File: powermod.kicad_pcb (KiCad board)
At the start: 4 copper layers, 27 x 18 mm, 21 parts, among them J1 Conn_02x07_Odd_Even, J2 Conn_02x07_Odd_Even, U1 TPS54260DGQ

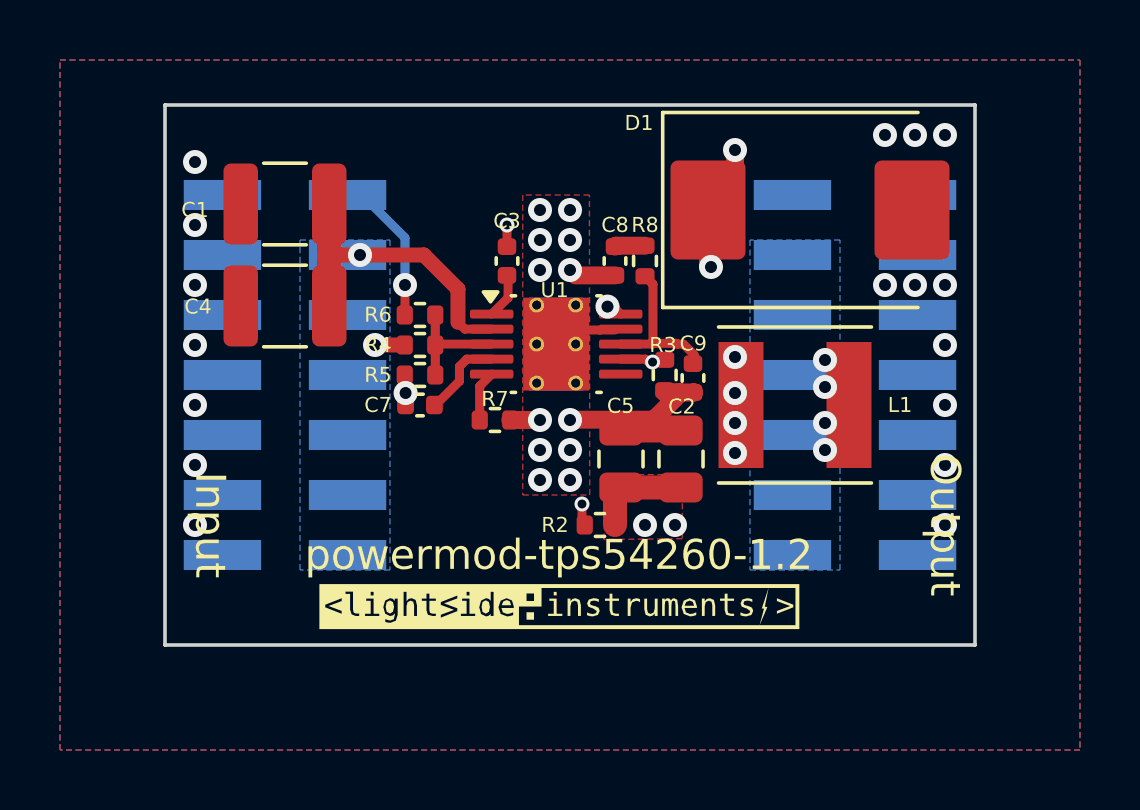
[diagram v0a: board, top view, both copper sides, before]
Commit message: feat: moved feedback resistor
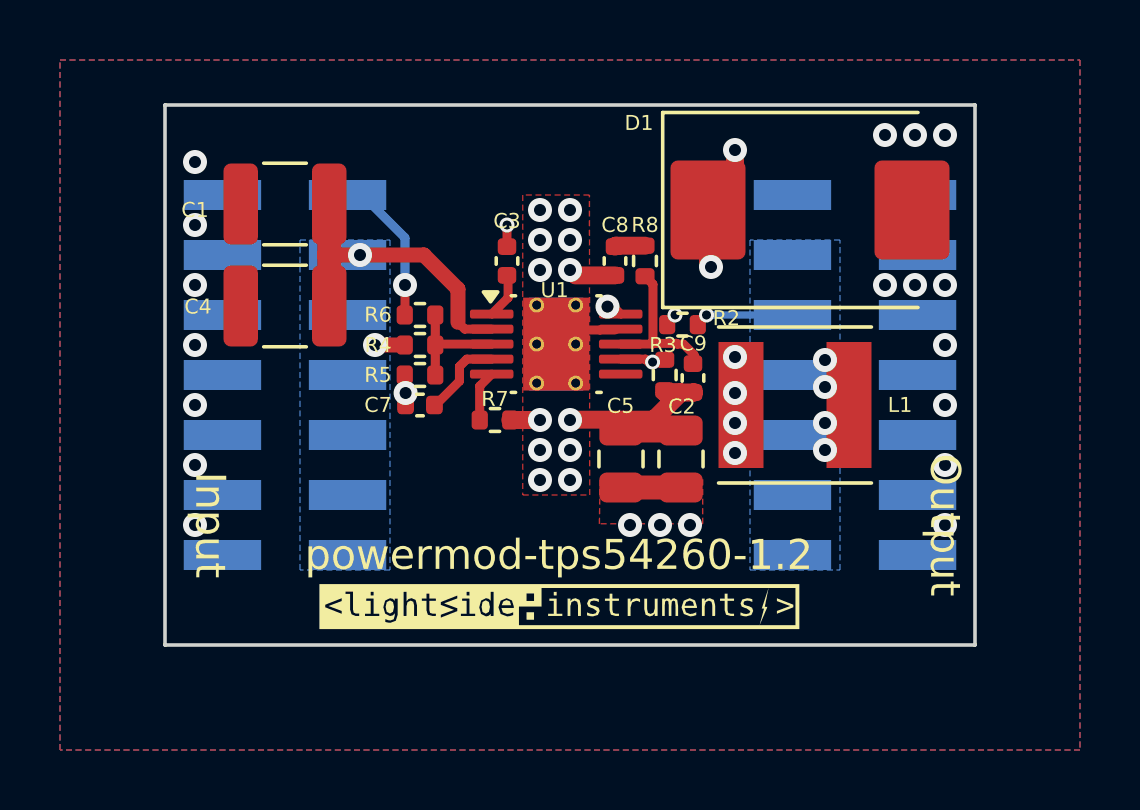
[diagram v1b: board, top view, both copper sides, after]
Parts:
- moved R2 7.22 mm to (33.2, 46.3)
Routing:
- net /FB: track 7.54 -> 2.98 mm
- net +5V: track 3.56 -> 5.54 mm, vias 6 -> 8
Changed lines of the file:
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@@
 	(footprint "Resistor_SMD:R_0402_1005Metric"
 		(layer "F.Cu")
-		(at 30.5 53 180)
+		(at 33.25 46.32 180)
 		(descr "Resistor SMD 0402 (1005 Metric), square (rectangular) end terminal, IPC_7351 nominal, (Body size source: IPC-SM-782 page 72, https://www.pcb-3d.com/wordpress/wp-content/uploads/ipc-sm-782a_amendment_1_and_2.pdf), generated with kicad-footprint-generator")
 		(tags "resistor")
 		(property "Reference" "R2"
-			(at 1.5 0 180)
+			(at -1.462373 0.213814 180)
 			(layer "F.SilkS")
 			(effects
@@
 		)
 		(property "Value" "52K"
-			(at 0 1.17 360)
+			(at 0 1.17 0)
 			(layer "F.Fab")
 			(effects
@@
 		)
 		(fp_text user "${REFERENCE}"
-			(at 0 0 360)
+			(at 0 0 0)
 			(layer "F.Fab")
 			(effects
@@
 		)
 		(property "Value" "56.2K"
-			(at 0 1.17 360)
+			(at 0 1.17 0)
 			(layer "F.Fab")
 			(effects
@@
 		)
 		(fp_text user "${REFERENCE}"
-			(at 0 0 360)
+			(at 0 0 0)
 			(layer "F.Fab")
 			(effects
@@
 		(tags "resistor")
 		(property "Reference" "R8"
-			(at -1.2 0 360)
+			(at -1.2 0 0)
 			(layer "F.SilkS")
 			(effects
@@
 		)
 		(property "Value" "0.025uF"
-			(at 0 1.16 360)
+			(at 0 1.16 0)
 			(layer "F.Fab")
 			(effects
@@
 		)
 		(fp_text user "${REFERENCE}"
-			(at 0 0 360)
+			(at 0 0 0)
 			(layer "F.Fab")
 			(effects
@@
 	)
 	(segment
-		(start 31 51.931971)
+		(start 31.331971 51.9)
 		(end 31.181971 51.75)
-		(width 0.8)
+		(width 0.5)
 		(layer "F.Cu")
 		(net 2)
 	)
 	(segment
-		(start 31 53)
-		(end 31 51.931971)
-		(width 0.8)
+		(start 33.767124 46.328938)
+		(end 34.05 46.046062)
+		(width 0.25)
 		(layer "F.Cu")
 		(net 2)
 	)
 	(segment
-		(start 31.331971 51.9)
+		(start 33.2 51.75)
 		(end 31.181971 51.75)
-		(width 0.5)
+		(width 0.8)
 		(layer "F.Cu")
 		(net 2)
 	)
 	(segment
-		(start 33.2 51.75)
-		(end 31.181971 51.75)
-		(width 0.8)
+		(start 34.05 46.046062)
+		(end 34.05 46)
+		(width 0.25)
 		(layer "F.Cu")
 		(net 2)
@@
 	)
 	(via
-		(at 33 53)
+		(at 38 47.5)
 		(size 0.8)
 		(drill 0.4)
 		(layers "F.Cu" "B.Cu")
-		(free yes)
 		(net 2)
 	)
 	(via
-		(at 38 47.5)
+		(at 33.5 53)
 		(size 0.8)
 		(drill 0.4)
 		(layers "F.Cu" "B.Cu")
+		(free yes)
 		(net 2)
 	)
 	(via
-		(at 32 53)
+		(at 32.5 53)
 		(size 0.8)
 		(drill 0.4)
 		(layers "F.Cu" "B.Cu")
+		(free yes)
 		(net 2)
 	)
@@
 	)
 	(via
+		(at 31.5 53)
+		(size 0.8)
+		(drill 0.4)
+		(layers "F.Cu" "B.Cu")
+		(free yes)
+		(net 2)
+	)
+	(via
+		(at 34.05 46)
+		(size 0.5)
+		(drill 0.3)
+		(layers "F.Cu" "B.Cu")
+		(net 2)
+	)
+	(via
 		(at 38 49.6)
 		(size 0.8)
@@
 	)
 	(segment
+		(start 34.05 46)
+		(end 36.915 46)
+		(width 0.25)
+		(layer "B.Cu")
+		(net 2)
+	)
+	(segment
 		(start 22.5 44)
 		(end 21.475 44)
@@
 	)
 	(segment
-		(start 32.879999 45.720001)
-		(end 34.2 44.4)
+		(start 30.75 45.720001)
+		(end 31.970001 44.5)
 		(width 0.5)
 		(layer "In2.Cu")
@@
 	)
 	(segment
-		(start 30.75 45.720001)
-		(end 32.879999 45.720001)
+		(start 31.970001 44.5)
+		(end 34.1 44.5)
+		(width 0.5)
+		(layer "In2.Cu")
+		(net 4)
+	)
+	(segment
+		(start 34.1 44.5)
+		(end 34.2 44.4)
 		(width 0.5)
 		(layer "In2.Cu")
@@
 	)
 	(segment
-		(start 29.9 52.3)
-		(end 29.9 52.92)
-		(width 0.3)
-		(layer "F.Cu")
-		(net 6)
-	)
-	(segment
-		(start 29.9 52.92)
-		(end 29.98 53)
-		(width 0.3)
-		(layer "F.Cu")
-		(net 6)
-	)
-	(segment
 		(start 32.118003 47.569883)
 		(end 32.01812 47.47)
@@
 	)
 	(via
-		(at 29.9 52.3)
+		(at 33 46)
 		(size 0.5)
 		(drill 0.3)
@@
 	)
 	(segment
-		(start 32.253287 47.569883)
-		(end 32.253287 49.946713)
+		(start 32.253287 46.746713)
+		(end 33 46)
 		(width 0.3)
 		(layer "In2.Cu")
@@
 	)
 	(segment
-		(start 32.253287 49.946713)
-		(end 29.9 52.3)
+		(start 32.253287 47.569883)
+		(end 32.253287 46.746713)
 		(width 0.3)
 		(layer "In2.Cu")
@@
 		(net_name "+5V")
 		(layer "F.Cu")
-		(hatch edge 0.508)
+		(hatch edge 0.5)
 		(priority 7)
-		(connect_pads yes
+		(connect_pads
 			(clearance 0.508)
 		)
-		(min_thickness 0.254)
+		(min_thickness 0.25)
 		(filled_areas_thickness no)
 		(fill yes
-			(thermal_gap 0.508)
-			(thermal_bridge_width 0.508)
+			(thermal_gap 0.5)
+			(thermal_bridge_width 0.5)
 		)
 		(polygon
 			(pts
-				(xy 31.038557 52.172268) (xy 31.687594 52.114433) (xy 31.771133 51.324021) (xy 33.242713 51.317595)
-				(xy 33.242713 53.45749) (xy 30.627285 53.483195) (xy 30.717251 52.165842)
+				(xy 30.5 51.5) (xy 33.922404 51.479986) (xy 33.922404 52.959548) (xy 30.480412 52.959548)
 			)
 		)

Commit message: fix: added missing trace
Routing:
- net /SW: track 21.7 -> 22.4 mm
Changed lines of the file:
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@@
+	)
+	(segment
+		(start 34.2 44.4)
+		(end 34.6 44.4)
+		(width 0.5)
+		(layer "In1.Cu")
+		(net 4)
 	)
 	(segment
@@
 		(layer "In1.Cu")
 		(net 4)
+	)
+	(segment
+		(start 34.6 44.4)
+		(end 34.75 44.25)
+		(width 0.5)
+		(layer "In1.Cu")
+		(net 4)

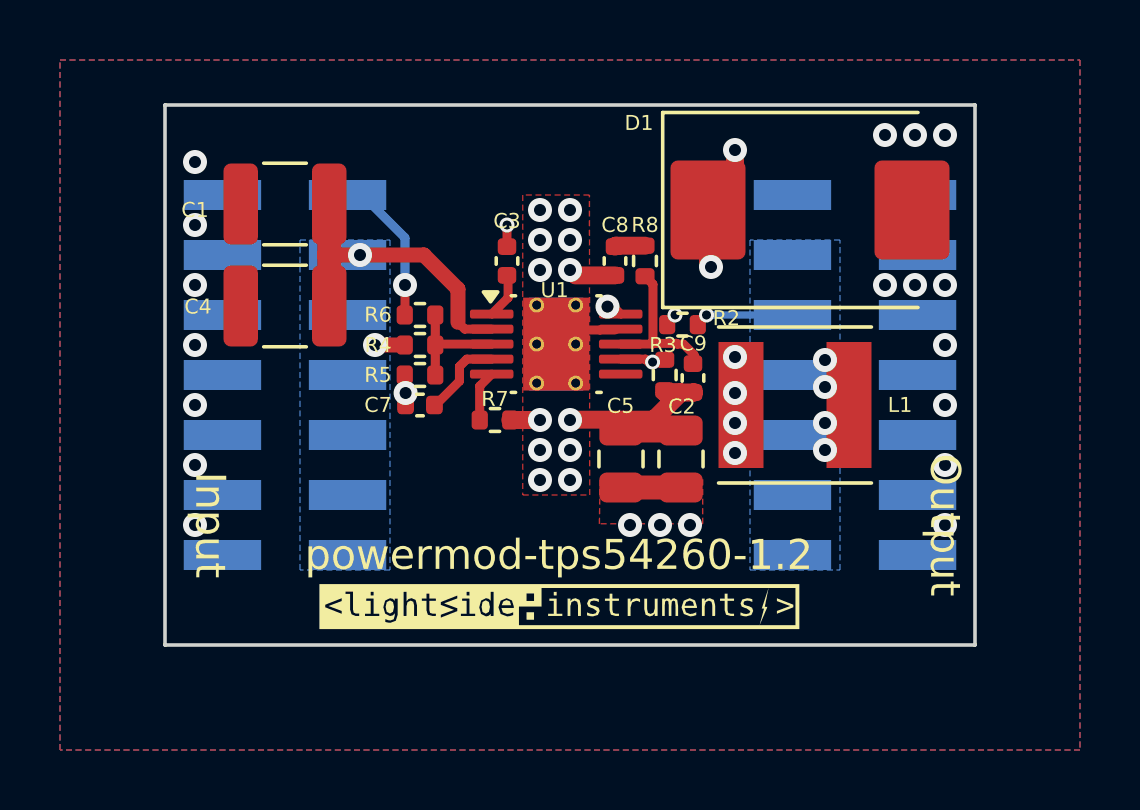
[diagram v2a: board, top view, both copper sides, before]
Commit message: fix: moved vias
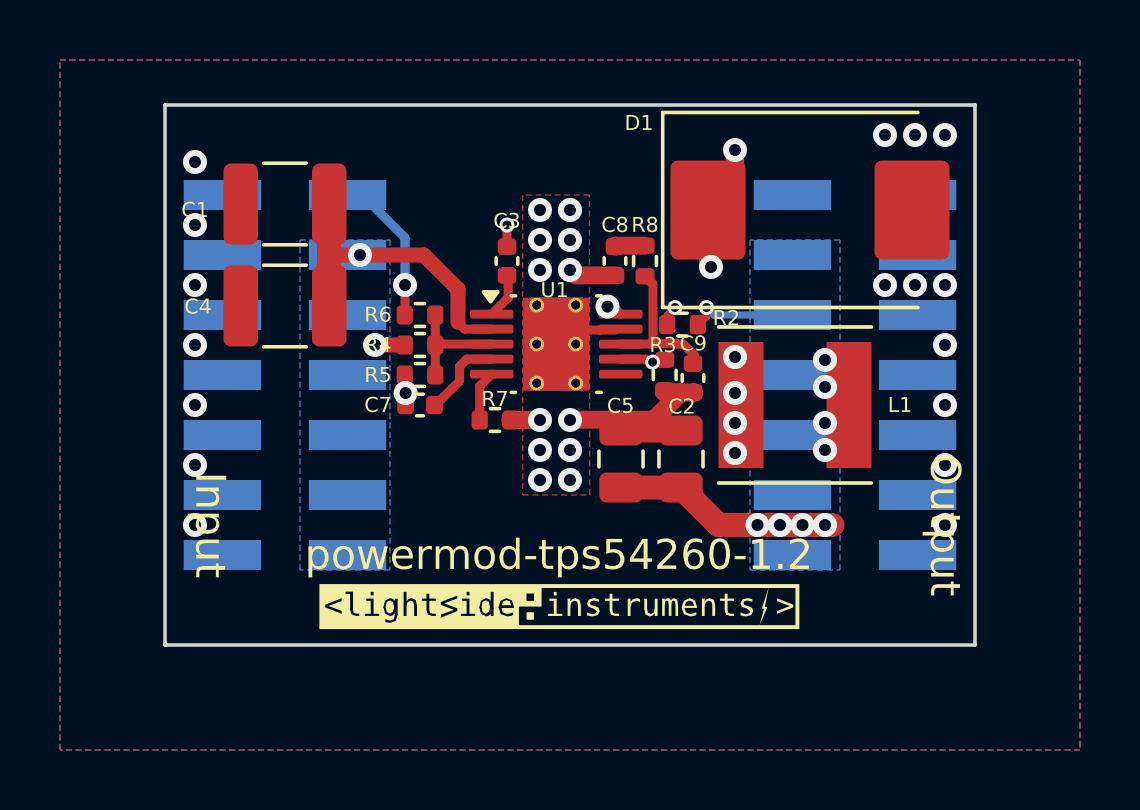
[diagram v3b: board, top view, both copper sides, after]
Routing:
- net +5V: track 5.54 -> 11.5 mm, vias 8 -> 9
- net /FB: track 2.98 -> 3.91 mm
- removed copper zone on F.Cu, net +5V
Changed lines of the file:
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@@
+	)
+	(segment
+		(start 38 53)
+		(end 38.25 53)
+		(width 0.8)
+		(layer "F.Cu")
+		(net 2)
+	)
+	(segment
+		(start 36.5 53)
+		(end 37.25 53)
+		(width 0.8)
+		(layer "F.Cu")
+		(net 2)
+	)
+	(segment
+		(start 34.05 45.75)
+		(end 34.05 46.046062)
+		(width 0.25)
+		(layer "F.Cu")
+		(net 2)
+	)
+	(segment
+		(start 35 53)
+		(end 35.75 53)
+		(width 0.8)
+		(layer "F.Cu")
+		(net 2)
+	)
+	(segment
+		(start 34.45 53)
+		(end 35 53)
+		(width 0.8)
+		(layer "F.Cu")
+		(net 2)
+	)
+	(segment
+		(start 37.25 53)
+		(end 38 53)
+		(width 0.8)
+		(layer "F.Cu")
+		(net 2)
+	)
+	(segment
+		(start 34.05 46.046062)
+		(end 33.767124 46.328938)
+		(width 0.25)
+		(layer "F.Cu")
+		(net 2)
 	)
 	(segment
@@
 	)
 	(segment
-		(start 33.767124 46.328938)
-		(end 34.05 46.046062)
-		(width 0.25)
+		(start 35.75 53)
+		(end 36.5 53)
+		(width 0.8)
+		(layer "F.Cu")
+		(net 2)
+	)
+	(segment
+		(start 33.2 51.75)
+		(end 34.45 53)
+		(width 0.8)
 		(layer "F.Cu")
 		(net 2)
@@
 		(net 2)
 	)
-	(segment
-		(start 34.05 46.046062)
-		(end 34.05 46)
-		(width 0.25)
-		(layer "F.Cu")
-		(net 2)
-	)
 	(via
 		(at 38 50.5)
@@
 	)
 	(via
-		(at 33.5 53)
-		(size 0.8)
-		(drill 0.4)
-		(layers "F.Cu" "B.Cu")
-		(free yes)
-		(net 2)
-	)
-	(via
-		(at 32.5 53)
-		(size 0.8)
-		(drill 0.4)
-		(layers "F.Cu" "B.Cu")
-		(free yes)
+		(at 37.25 53)
+		(size 0.8)
+		(drill 0.4)
+		(layers "F.Cu" "B.Cu")
+		(net 2)
+	)
+	(via
+		(at 36.5 53)
+		(size 0.8)
+		(drill 0.4)
+		(layers "F.Cu" "B.Cu")
+		(net 2)
+	)
+	(via
+		(at 38 53)
+		(size 0.8)
+		(drill 0.4)
+		(layers "F.Cu" "B.Cu")
+		(net 2)
+	)
+	(via
+		(at 35.75 53)
+		(size 0.8)
+		(drill 0.4)
+		(layers "F.Cu" "B.Cu")
 		(net 2)
 	)
@@
 	)
 	(via
-		(at 31.5 53)
-		(size 0.8)
-		(drill 0.4)
-		(layers "F.Cu" "B.Cu")
-		(free yes)
-		(net 2)
-	)
-	(via
-		(at 34.05 46)
+		(at 34.05 45.75)
 		(size 0.5)
 		(drill 0.3)
@@
 	)
 	(segment
-		(start 34.05 46)
+		(start 34.3 46)
 		(end 36.915 46)
 		(width 0.25)
@@
 	)
 	(segment
+		(start 34.05 45.75)
+		(end 34.3 46)
+		(width 0.25)
+		(layer "B.Cu")
+		(net 2)
+	)
+	(segment
 		(start 22.5 44)
 		(end 21.475 44)
@@
 	)
 	(segment
+		(start 32.74 46.32)
+		(end 32.74 46.01)
+		(width 0.25)
+		(layer "F.Cu")
+		(net 6)
+	)
+	(segment
+		(start 32.74 46.01)
+		(end 33 45.75)
+		(width 0.25)
+		(layer "F.Cu")
+		(net 6)
+	)
+	(segment
 		(start 32.118003 47.569883)
 		(end 32.01812 47.47)
@@
 	)
 	(via
-		(at 33 46)
+		(at 33 45.75)
 		(size 0.5)
 		(drill 0.3)
@@
 	)
 	(segment
-		(start 32.253287 46.746713)
-		(end 33 46)
+		(start 33 45.75)
+		(end 32.253287 46.496713)
 		(width 0.3)
 		(layer "In2.Cu")
@@
 	)
 	(segment
-		(start 32.253287 47.569883)
-		(end 32.253287 46.746713)
+		(start 32.253287 46.496713)
+		(end 32.253287 47.569883)
 		(width 0.3)
 		(layer "In2.Cu")
@@
 			(pts
 				(xy 12.5 37.5) (xy 46.5 37.5) (xy 46.5 60.5) (xy 12.5 60.5)
-			)
-		)
-	)
-	(zone
-		(net 2)
-		(net_name "+5V")
-		(layer "F.Cu")
-		(hatch edge 0.5)
-		(priority 7)
-		(connect_pads
-			(clearance 0.508)
-		)
-		(min_thickness 0.25)
-		(filled_areas_thickness no)
-		(fill yes
-			(thermal_gap 0.5)
-			(thermal_bridge_width 0.5)
-		)
-		(polygon
-			(pts
-				(xy 30.5 51.5) (xy 33.922404 51.479986) (xy 33.922404 52.959548) (xy 30.480412 52.959548)
 			)
 		)
@@
 		(polygon
 			(pts
-				(xy 34.5 40) (xy 35.5 40) (xy 35.5 49) (xy 34.5 49)
+				(xy 34.5 40) (xy 35.5 40) (xy 35.5 51) (xy 34.5 51)
 			)
 		)

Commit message: fix: updated the version
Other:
- board text added: "powermod-tps54260-1.3"
- board text removed: "powermod-tps54260-1.2"
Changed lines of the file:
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@@
 		)
 	)
-	(gr_text "powermod-tps54260-1.2"
+	(gr_text "powermod-tps54260-1.3"
 		(at 29.129989 54 0)
 		(layer "F.SilkS")
@@
 	)
 	(segment
+		(start 32.160854 46.838589)
+		(end 32.26686 46.944595)
+		(width 0.2)
+		(layer "F.Cu")
+		(net 14)
+	)
+	(segment
 		(start 33.28 46.97)
 		(end 33.071533 46.97)
@@
 	)
 	(segment
-		(start 32.265 44.975)
-		(end 32.265 46.87186)
-		(width 0.3)
+		(start 32.160854 45.079146)
+		(end 32.160854 46.838589)
+		(width 0.2)
 		(layer "F.Cu")
 		(net 14)
@@
 	)
 	(segment
-		(start 32.265 46.87186)
-		(end 32.229562 46.907298)
-		(width 0.3)
-		(layer "F.Cu")
-		(net 14)
-	)
-	(segment
 		(start 32.26686 46.944595)
 		(end 32.241455 46.97)
@@
 	)
 	(segment
+		(start 32 44.71)
+		(end 32.160854 44.870854)
+		(width 0.3)
+		(layer "F.Cu")
+		(net 14)
+	)
+	(segment
 		(start 33.046128 46.944595)
 		(end 32.26686 46.944595)
@@
 	)
 	(segment
-		(start 32 44.71)
-		(end 32.265 44.975)
-		(width 0.3)
-		(layer "F.Cu")
-		(net 14)
-	)
-	(segment
 		(start 33.635483 47.611462)
 		(end 33.635483 47.325483)
 		(width 0.3)
 		(layer "F.Cu")
+		(net 14)
+	)
+	(segment
+		(start 32.160854 44.870854)
+		(end 32.160854 45.5)
+		(width 0.3)
+		(layer "F.Cu")

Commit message: feat: 1.4
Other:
- board text added: "powermod-tps54260-1.4"
- board text removed: "powermod-tps54260-1.3"
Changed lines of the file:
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@@
 		)
 	)
-	(gr_text "powermod-tps54260-1.3"
+	(gr_text "powermod-tps54260-1.4"
 		(at 29.129989 54 0)
 		(layer "F.SilkS")
